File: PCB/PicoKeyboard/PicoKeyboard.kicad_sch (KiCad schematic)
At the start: 1 part, among them U1 Raspberry_Pi_Pico

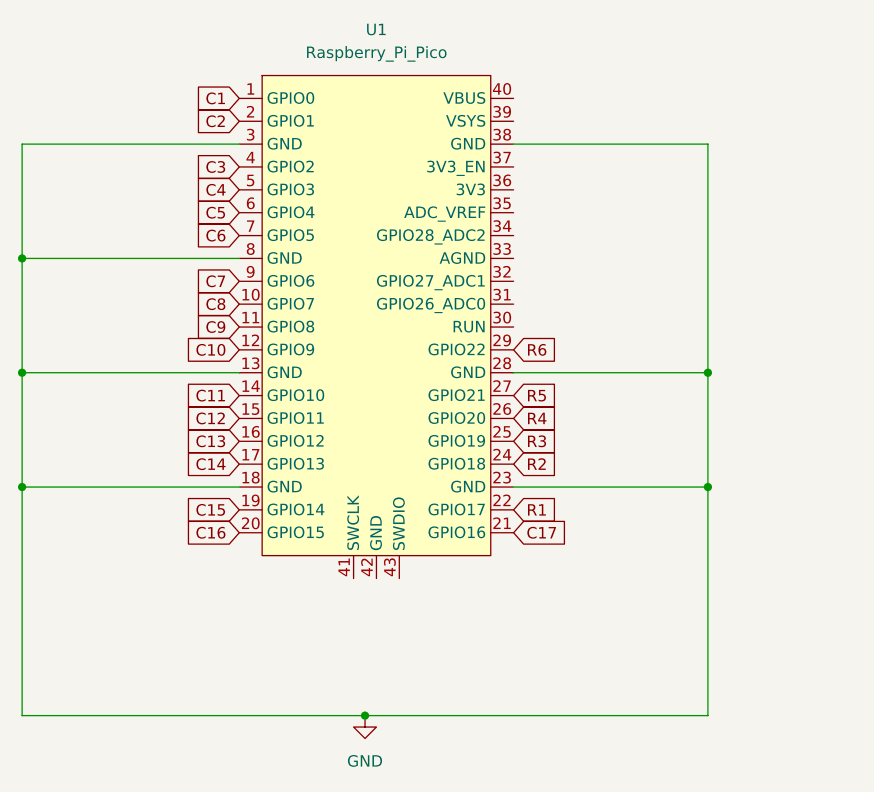
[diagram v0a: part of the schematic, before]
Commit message: Completed prototype design for my custom keyboard
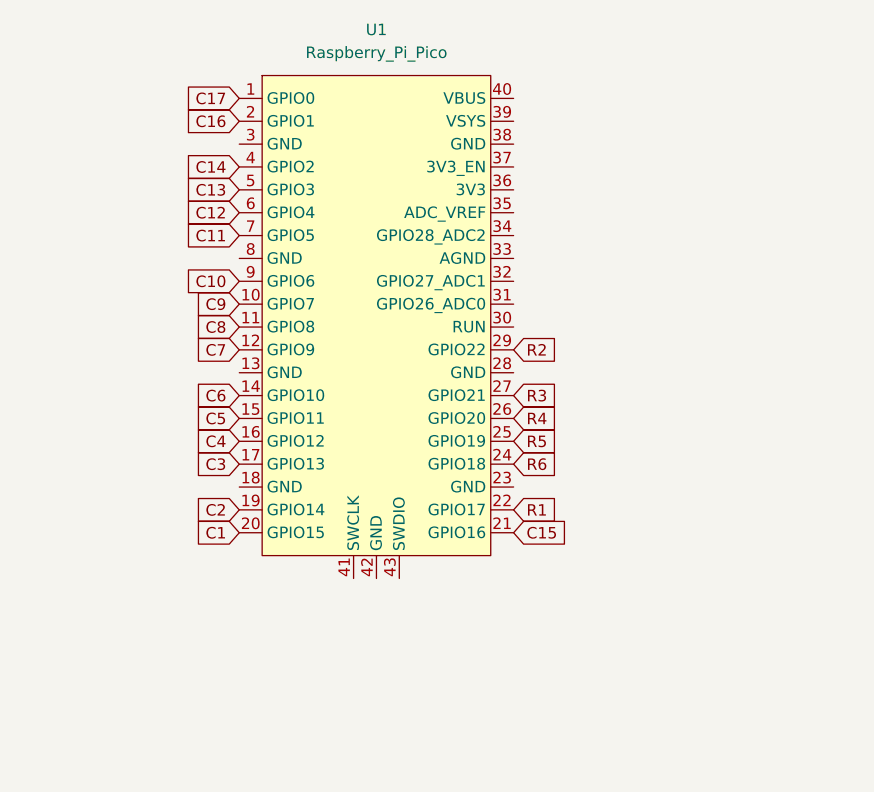
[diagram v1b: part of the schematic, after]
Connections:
- net C1: now also U1.20 (GPIO15); no longer U1.1 (GPIO0)
- net C10: now also U1.9 (GPIO6); no longer U1.12 (GPIO9)
- net C11: now also U1.7 (GPIO5); no longer U1.14 (GPIO10)
- net C12: now also U1.6 (GPIO4); no longer U1.15 (GPIO11)
- net C13: now also U1.5 (GPIO3); no longer U1.16 (GPIO12)
- net C14: now also U1.4 (GPIO2); no longer U1.17 (GPIO13)
- net C15: now also U1.21 (GPIO16); no longer U1.19 (GPIO14)
- net C16: now also U1.2 (GPIO1); no longer U1.20 (GPIO15)
- net C17: now also U1.1 (GPIO0); no longer U1.21 (GPIO16)
- net C2: now also U1.19 (GPIO14); no longer U1.2 (GPIO1)
- net C3: now also U1.17 (GPIO13); no longer U1.4 (GPIO2)
- net C4: now also U1.16 (GPIO12); no longer U1.5 (GPIO3)
- net C5: now also U1.15 (GPIO11); no longer U1.6 (GPIO4)
- net C6: now also U1.14 (GPIO10); no longer U1.7 (GPIO5)
- net C7: now also U1.12 (GPIO9); no longer U1.9 (GPIO6)
- net C8: now also U1.11 (GPIO8); no longer U1.10 (GPIO7)
- net C9: now also U1.10 (GPIO7); no longer U1.11 (GPIO8)
- net R2: now also U1.29 (GPIO22); no longer U1.24 (GPIO18)
- net R3: now also U1.27 (GPIO21); no longer U1.25 (GPIO19)
- net R5: now also U1.25 (GPIO19); no longer U1.27 (GPIO21)
- net R6: now also U1.24 (GPIO18); no longer U1.29 (GPIO22)
- removed net GND: U1.13 (GND), U1.18 (GND), U1.23 (GND), U1.28 (GND), U1.3 (GND), U1.38 (GND), U1.8 (GND)

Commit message: Rewired
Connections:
- net C1: now also U1.29 (GPIO22); no longer U1.20 (GPIO15)
- net C10: now also U1.15 (GPIO11); no longer U1.9 (GPIO6)
- net C11: now also U1.16 (GPIO12); no longer U1.7 (GPIO5)
- net C12: now also U1.17 (GPIO13); no longer U1.6 (GPIO4)
- net C13: now also U1.19 (GPIO14); no longer U1.5 (GPIO3)
- net C14: now also U1.20 (GPIO15); no longer U1.4 (GPIO2)
- net C15: now also U1.10 (GPIO7); no longer U1.21 (GPIO16)
- net C16: now also U1.9 (GPIO6); no longer U1.2 (GPIO1)
- net C17: now also U1.7 (GPIO5); no longer U1.1 (GPIO0)
- net C2: now also U1.27 (GPIO21); no longer U1.19 (GPIO14)
- net C3: now also U1.26 (GPIO20); no longer U1.17 (GPIO13)
- net C4: now also U1.25 (GPIO19); no longer U1.16 (GPIO12)
- net C5: now also U1.24 (GPIO18); no longer U1.15 (GPIO11)
- net C6: now also U1.22 (GPIO17); no longer U1.14 (GPIO10)
- net C7: now also U1.21 (GPIO16); no longer U1.12 (GPIO9)
- net C8: now also U1.12 (GPIO9); no longer U1.11 (GPIO8)
- net C9: now also U1.14 (GPIO10); no longer U1.10 (GPIO7)
- net R1: now also U1.11 (GPIO8); no longer U1.22 (GPIO17)
- net R2: now also U1.6 (GPIO4); no longer U1.29 (GPIO22)
- net R3: now also U1.5 (GPIO3); no longer U1.27 (GPIO21)
- net R4: now also U1.4 (GPIO2); no longer U1.26 (GPIO20)
- net R5: now also U1.2 (GPIO1); no longer U1.25 (GPIO19)
- net R6: now also U1.1 (GPIO0); no longer U1.24 (GPIO18)

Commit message: New layout
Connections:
- net C13 is gone; now on net R1: U1.19 (GPIO14)
- net C14 is gone; now on net R2: U1.20 (GPIO15)
- net C15 is gone; now on net C7: U1.10 (GPIO7)
- net C16 is gone; now on net C6: U1.9 (GPIO6)
- net C17 is gone; now on net C5: U1.7 (GPIO5)
- net C1: now also U1.2 (GPIO1); no longer U1.29 (GPIO22)
- net C10: now also U1.14 (GPIO10); no longer U1.15 (GPIO11)
- net C11: now also U1.15 (GPIO11); no longer U1.16 (GPIO12)
- net C12: now also U1.16 (GPIO12); no longer U1.17 (GPIO13)
- net C2: now also U1.4 (GPIO2); no longer U1.27 (GPIO21)
- net C3: now also U1.5 (GPIO3); no longer U1.26 (GPIO20)
- net C4: now also U1.6 (GPIO4); no longer U1.25 (GPIO19)
- net C5: no longer U1.24 (GPIO18)
- net C6: no longer U1.22 (GPIO17)
- net C7: no longer U1.21 (GPIO16)
- net C8: now also U1.11 (GPIO8); no longer U1.12 (GPIO9)
- net C9: now also U1.12 (GPIO9); no longer U1.14 (GPIO10)
- net R1: no longer U1.11 (GPIO8)
- net R2: no longer U1.6 (GPIO4)
- net R3: now also U1.21 (GPIO16); no longer U1.5 (GPIO3)
- net R4: now also U1.22 (GPIO17); no longer U1.4 (GPIO2)
- net R5: now also U1.24 (GPIO18); no longer U1.2 (GPIO1)
- net R6 renamed C0
- new net R0: U1.17 (GPIO13)
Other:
- moved on the sheet: U1

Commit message: Complete wiring
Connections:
- net R3: now also U1.24 (GPIO18); no longer U1.21 (GPIO16)
- net R5: now also U1.21 (GPIO16); no longer U1.24 (GPIO18)
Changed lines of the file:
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@@
 	(global_label "R5"
 		(shape input)
-		(at 137.16 100.33 0)
+		(at 137.16 107.95 0)
 		(fields_autoplaced yes)
 		(effects
@@
 		)
 		(property "Intersheetrefs" "${INTERSHEET_REFS}"
-			(at 142.6247 100.33 0)
+			(at 142.6247 107.95 0)
 			(effects
 				(font
@@
 	(global_label "R3"
 		(shape input)
-		(at 137.16 107.95 0)
+		(at 137.16 100.33 0)
 		(fields_autoplaced yes)
 		(effects
@@
 		)
 		(property "Intersheetrefs" "${INTERSHEET_REFS}"
-			(at 142.6247 107.95 0)
+			(at 142.6247 100.33 0)
 			(effects
 				(font

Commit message: Change layout
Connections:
- net R3: now also U1.22 (GPIO17); no longer U1.24 (GPIO18)
- net R4: now also U1.21 (GPIO16); no longer U1.22 (GPIO17)
- net R5: now also U1.24 (GPIO18); no longer U1.21 (GPIO16)
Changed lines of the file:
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@@
 	(global_label "R4"
 		(shape input)
-		(at 137.16 105.41 0)
+		(at 137.16 107.95 0)
 		(fields_autoplaced yes)
 		(effects
@@
 		)
 		(property "Intersheetrefs" "${INTERSHEET_REFS}"
-			(at 142.6247 105.41 0)
+			(at 142.6247 107.95 0)
 			(effects
 				(font
@@
 	(global_label "R5"
 		(shape input)
-		(at 137.16 107.95 0)
+		(at 137.16 100.33 0)
 		(fields_autoplaced yes)
 		(effects
@@
 		)
 		(property "Intersheetrefs" "${INTERSHEET_REFS}"
-			(at 142.6247 107.95 0)
+			(at 142.6247 100.33 0)
 			(effects
 				(font
@@
 	(global_label "R3"
 		(shape input)
-		(at 137.16 100.33 0)
+		(at 137.16 105.41 0)
 		(fields_autoplaced yes)
 		(effects
@@
 		)
 		(property "Intersheetrefs" "${INTERSHEET_REFS}"
-			(at 142.6247 100.33 0)
+			(at 142.6247 105.41 0)
 			(effects
 				(font

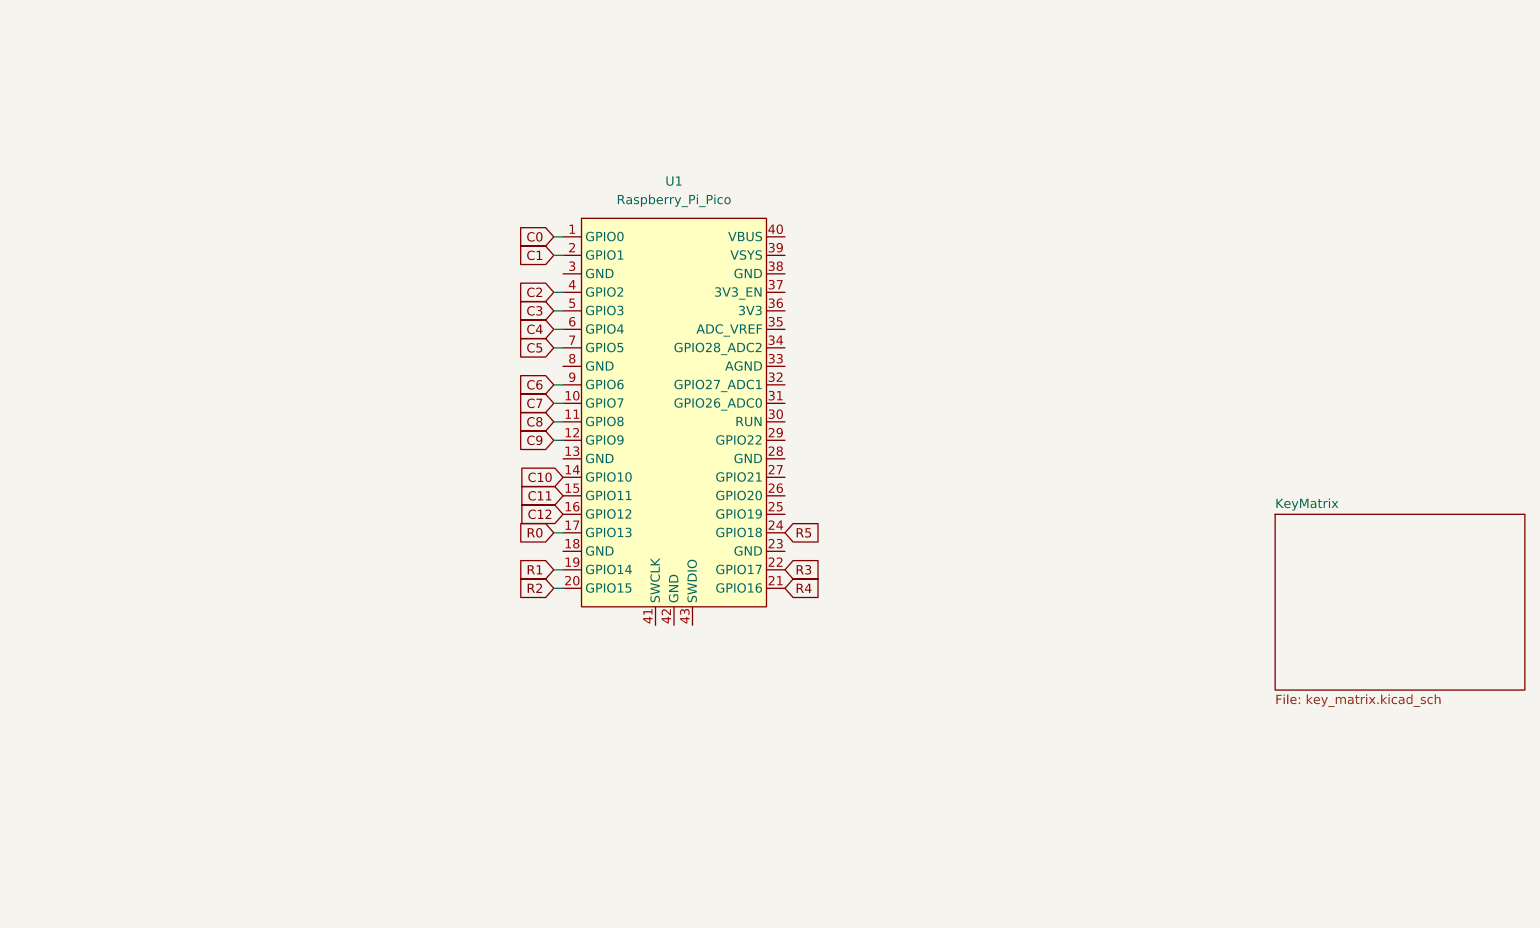
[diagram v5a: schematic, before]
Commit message: Add Usb C header and XH 2.54 header
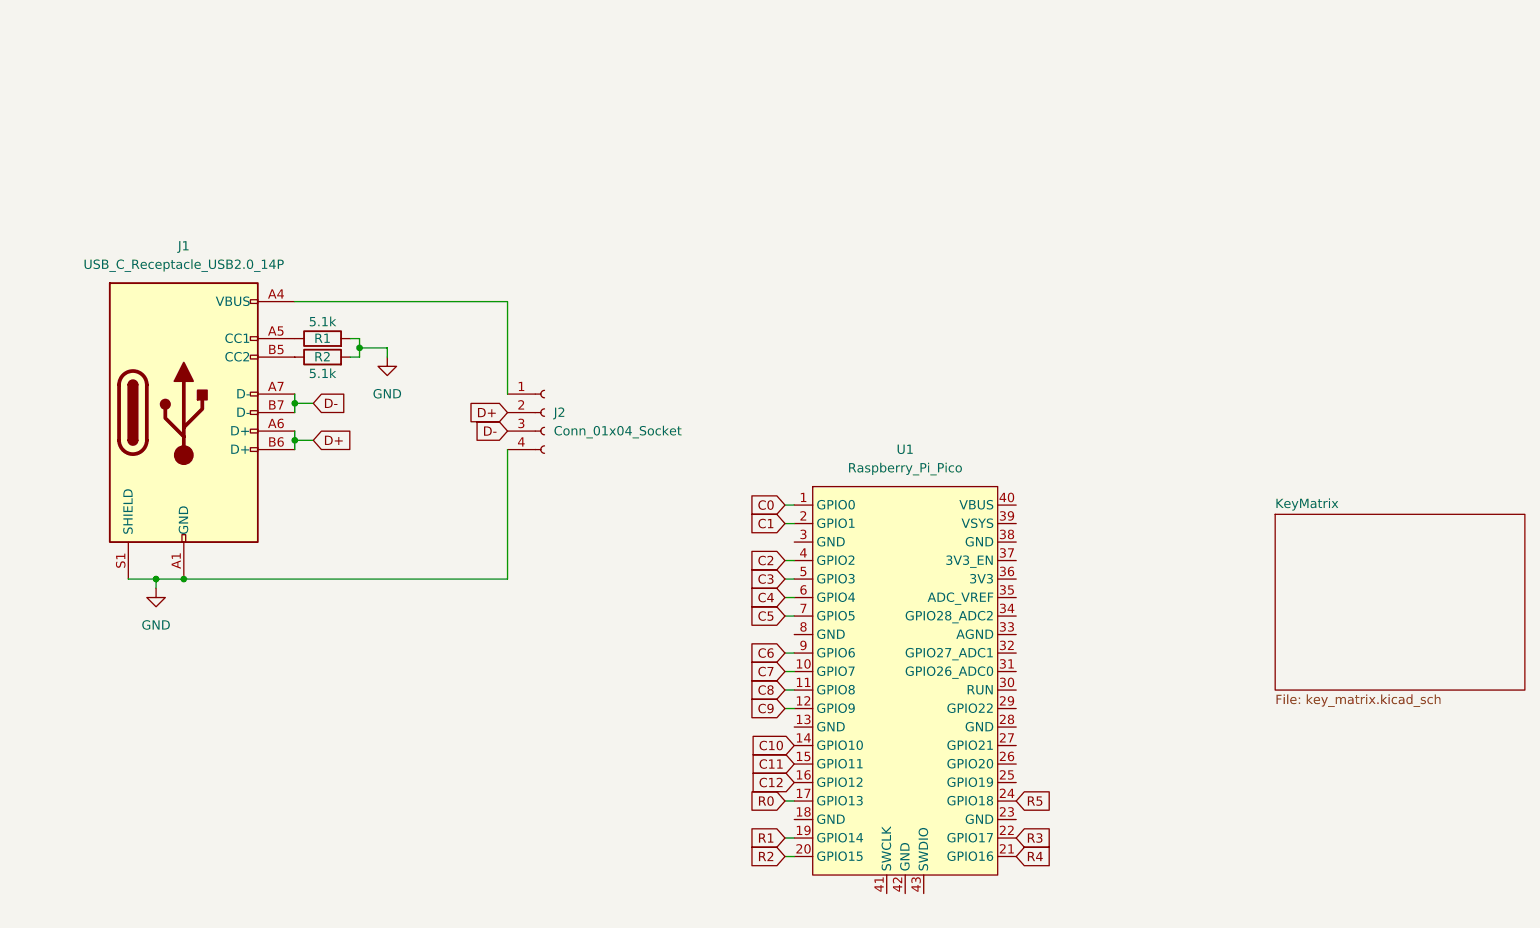
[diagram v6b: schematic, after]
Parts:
- added J1: USB_C_Receptacle_USB2.0_14P, Connector_USB:USB_C_Receptacle_GCT_USB4085, symbol Connector:USB_C_Receptacle_USB2.0_14P
- added J2: Conn_01x04_Socket, Connector_PinHeader_2.54mm:PinHeader_1x04_P2.54mm_Vertical, symbol Connector:Conn_01x04_Socket
- added R1, R2: 5.1k, Resistor_SMD:R_0612_1632Metric_Pad1.18x3.40mm_HandSolder, symbol ScottoKeebs:Placeholder_Resistor
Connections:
- new net: J1.A5 (CC1), R1.1
- new net: J1.A4 (VBUS), J1.A9 (VBUS), J1.B4 (VBUS), J1.B9 (VBUS), J2.1 (Pin_1)
- new net: J1.B5 (CC2), R2.1
- new net D+: J1.A6 (D+), J1.B6 (D+), J2.2 (Pin_2)
- new net D-: J1.A7 (D-), J1.B7 (D-), J2.3 (Pin_3)
- new net GND: J1.A1 (GND), J1.A12 (GND), J1.B1 (GND), J1.B12 (GND), J1.S1 (SHIELD), J2.4 (Pin_4), R1.2, R2.2
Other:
- moved on the sheet: U1

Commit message: Fix
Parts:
- R1, R2: footprint Resistor_SMD:R_0612_1632Metric_Pad1.18x3.40mm_HandSolder -> Resistor_SMD:R_0201_0603Metric_Pad0.64x0.40mm_HandSolder
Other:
- moved on the sheet: J1, J2, R1, R2, U1

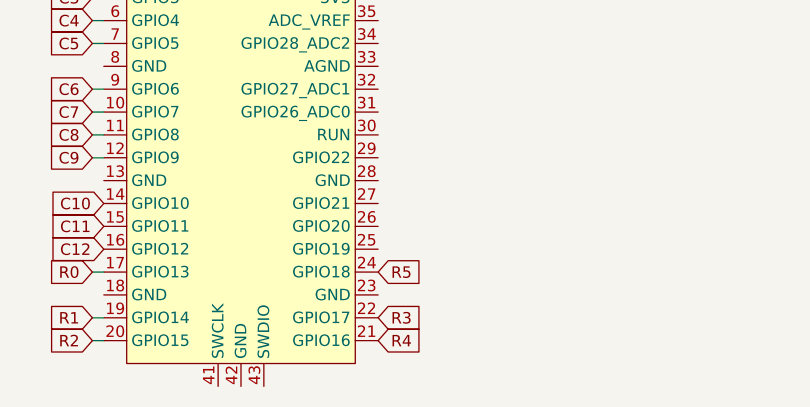
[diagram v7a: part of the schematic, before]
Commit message: Change gpio pin
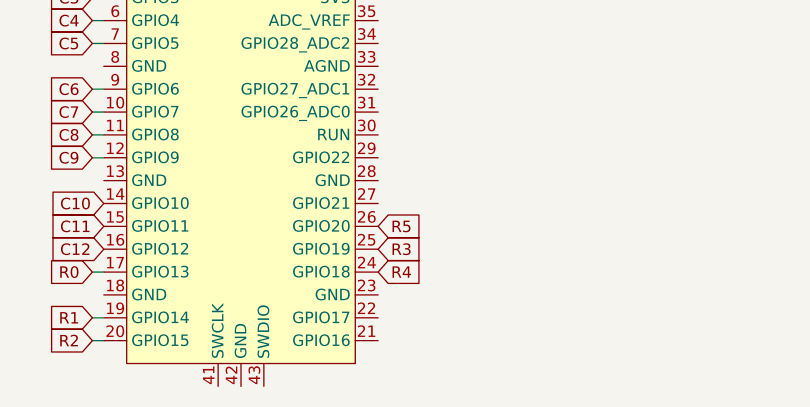
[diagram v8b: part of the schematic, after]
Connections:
- net R3: now also U1.25 (GPIO19); no longer U1.22 (GPIO17)
- net R4: now also U1.24 (GPIO18); no longer U1.21 (GPIO16)
- net R5: now also U1.26 (GPIO20); no longer U1.24 (GPIO18)
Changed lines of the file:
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@@
 	(global_label "R4"
 		(shape input)
-		(at 87.63 147.32 0)
+		(at 87.63 139.7 0)
 		(fields_autoplaced yes)
 		(effects
@@
 		)
 		(property "Intersheetrefs" "${INTERSHEET_REFS}"
-			(at 93.0947 147.32 0)
+			(at 93.0947 139.7 0)
 			(effects
 				(font
@@
 	(global_label "R5"
 		(shape input)
-		(at 87.63 139.7 0)
+		(at 87.63 134.62 0)
 		(fields_autoplaced yes)
 		(effects
@@
 		)
 		(property "Intersheetrefs" "${INTERSHEET_REFS}"
-			(at 93.0947 139.7 0)
+			(at 93.0947 134.62 0)
 			(effects
 				(font
@@
 	(global_label "R3"
 		(shape input)
-		(at 87.63 144.78 0)
+		(at 87.63 137.16 0)
 		(fields_autoplaced yes)
 		(effects
@@
 		)
 		(property "Intersheetrefs" "${INTERSHEET_REFS}"
-			(at 93.0947 144.78 0)
+			(at 93.0947 137.16 0)
 			(effects
 				(font
